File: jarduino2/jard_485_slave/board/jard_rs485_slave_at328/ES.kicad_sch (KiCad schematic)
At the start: 28 parts

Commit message: Re-routage en gagnant de la place (à finir)
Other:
- company: (none) -> BPC
- title: (none) -> Carte de commande d'un Oya par RS485
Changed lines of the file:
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@@
 (kicad_sch (version 20230121) (generator eeschema)
   (paper "A4")
+  (title_block
+    (title "Carte de commande d'un Oya par RS485")
+    (date "2024-03-29")
+    (rev "D0")
+    (company "BPC")
+    (comment 1 "Technologie CMD basée sur ATMEGA328")
+    (comment 2 "Monitoring de tension d'alimentation")
+    (comment 3 "1 sortie 12V/5A - 2 entrées TOR - 1 débimètre - 1 LED - Temp -RS485")
+  )
   (junction (at 60.96 87.63) (diameter 0) (color 0 0 0 0)
   )

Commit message: Petites coquilles de dossier
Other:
- title: Carte de commande d'un Oya par RS485 -> Carte de commande d'un OYA par RS485
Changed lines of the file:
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@@
   (paper "A4")
   (title_block
-    (title "Carte de commande d'un Oya par RS485")
+    (title "Carte de commande d'un OYA par RS485")
     (date "2024-03-29")
     (rev "D0")
     (company "BPC")
-    (comment 1 "Technologie CMD basée sur ATMEGA328")
+    (comment 1 "Technologie CMS basée sur ATMEGA328")
     (comment 2 "Monitoring de tension d'alimentation")
-    (comment 3 "1 sortie 12V/5A - 2 entrées TOR - 1 débimètre - 1 LED - Temp -RS485")
+    (comment 3 "1 sortie 12V/5A - 2 entrées TOR - 1 débimètre - 1 LED - Temp - RS485")
   )
   (junction (at 60.96 87.63) (diameter 0) (color 0 0 0 0)

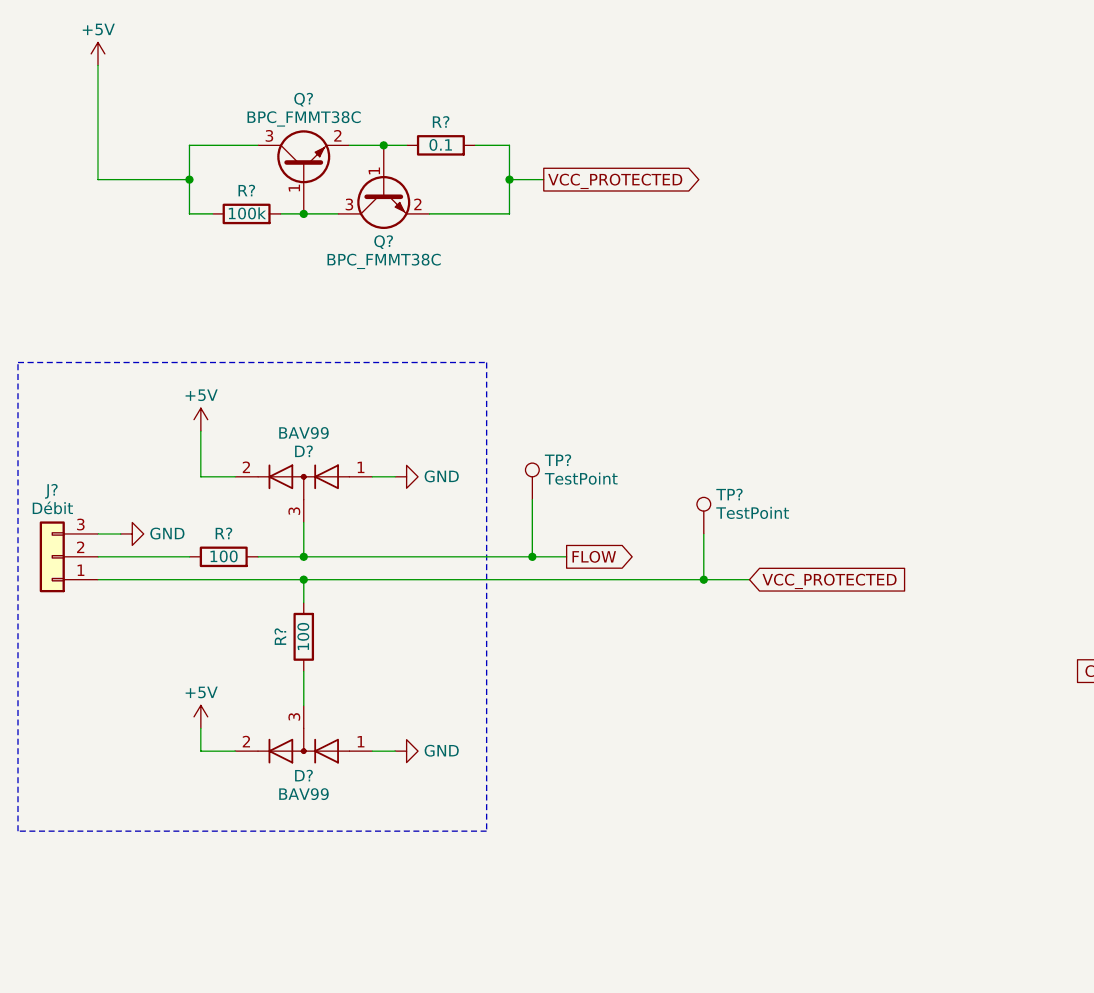
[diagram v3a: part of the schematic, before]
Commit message: Suite revue: - Retrait limiteur de courant NOK pour flowmeter - Résolution des erreurs PCB
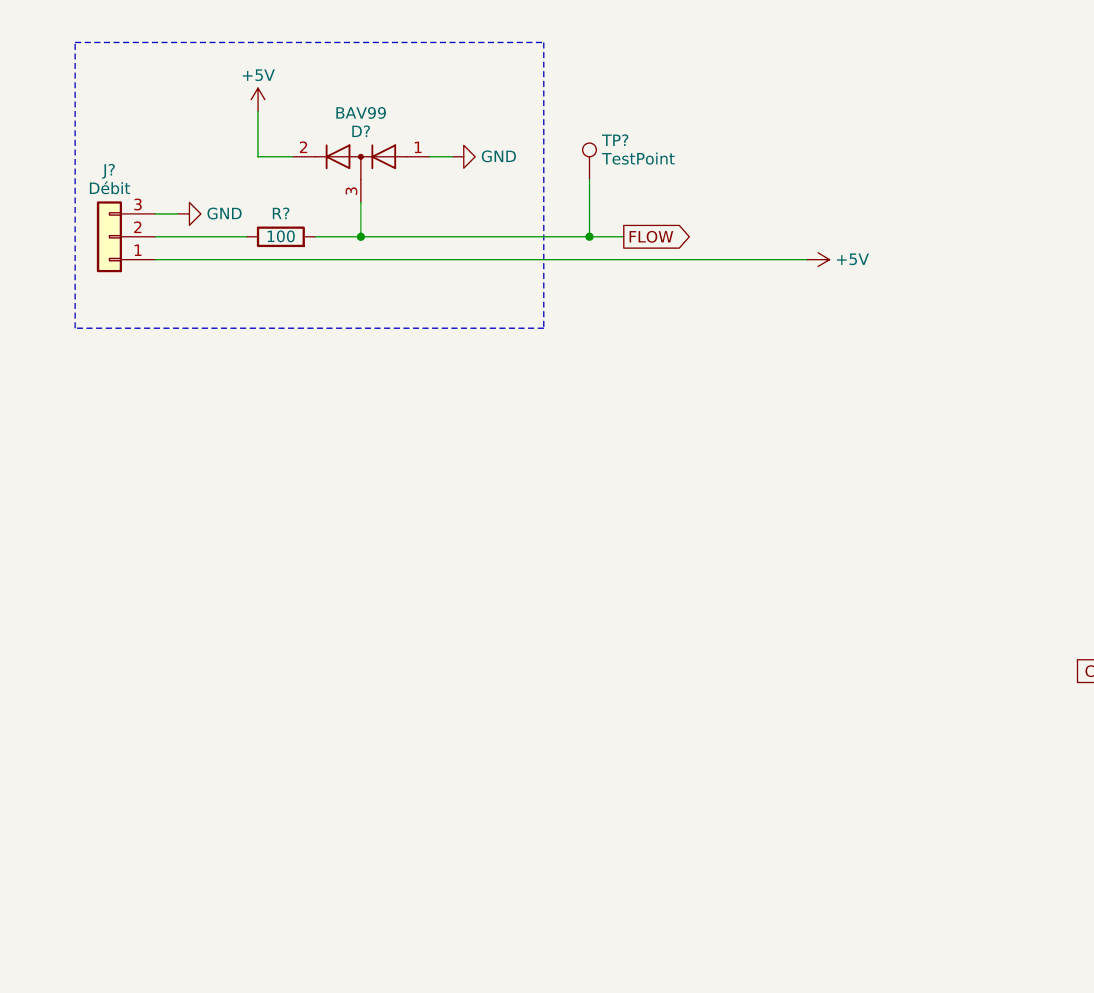
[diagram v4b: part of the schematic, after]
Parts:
- removed D?: BAV99, Package_TO_SOT_SMD:SOT-23, symbol Diode:BAV99
- removed Q? (x2): BPC_FMMT38C, bpc:BPC_SOT-23-3, symbol bpc:BPC_FMMT38C
- removed R?: 100, Resistor_SMD:R_0805_2012Metric_Pad1.20x1.40mm_HandSolder, symbol Device:R
- removed R?: 100k, Resistor_SMD:R_0805_2012Metric_Pad1.20x1.40mm_HandSolder, symbol Device:R
- removed R?: 0.1, Resistor_SMD:R_0805_2012Metric_Pad1.20x1.40mm_HandSolder, symbol Device:R
- removed TP?: TestPoint, TestPoint:TestPoint_Pad_D1.5mm, symbol Connector:TestPoint
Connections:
- net VCC_PROTECTED is gone; now on net +5V: J?.1 (Pin_1)
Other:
- title: Carte de commande d'un OYA par RS485 -> Carte de commande d'un OYA - Esclave RS485
- moved on the sheet: D?, J?, R?, TP?

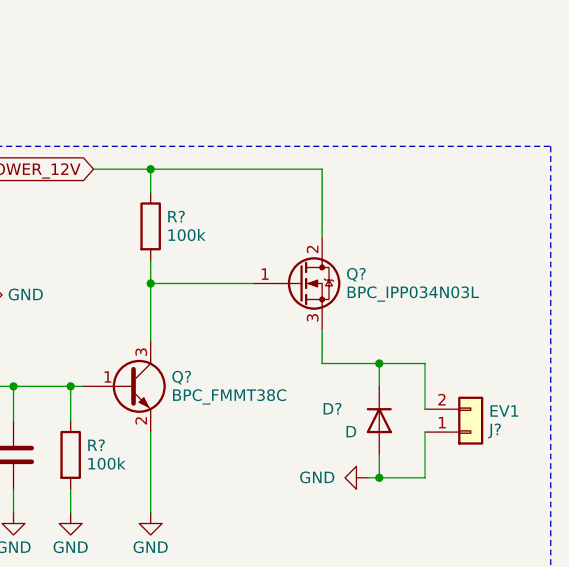
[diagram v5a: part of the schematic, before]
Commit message: Correction erreur de MOS (N au lieu de P) + Saisie complete de la BOM
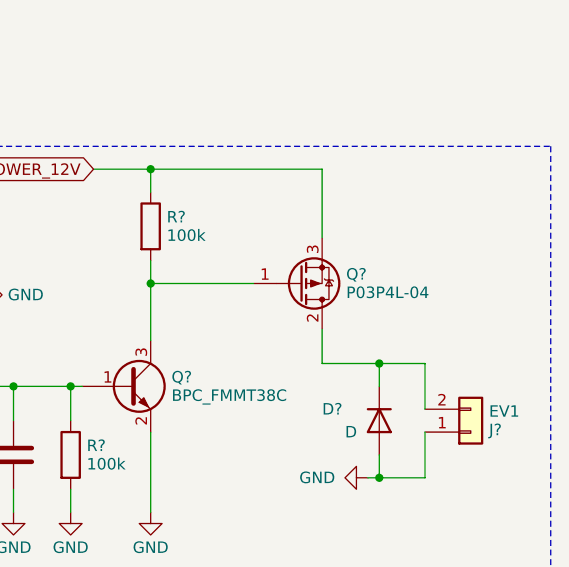
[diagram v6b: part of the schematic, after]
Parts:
- C?: Fabricant (none) -> KEMET; Fournisseur (none) -> Farnell; RefFabricant (none) -> C0603X102J5GACAUTO; RefFournisseur (none) -> 2219417
- D? (x4): Fabricant (none) -> MULTICOMP PRO; Fournisseur (none) -> Farnell; RefFabricant (none) -> BAV99; RefFournisseur (none) -> 2675152
- D?: Fabricant (none) -> MULTICOMP PRO; Fournisseur (none) -> Farnell; RefFabricant (none) -> 1N4007G; RefFournisseur (none) -> 2675047
- J? (x2): Fabricant (none) -> PHOENIX CONTACT; Fournisseur (none) -> Farnell; RefFabricant (none) -> 1725669; RefFournisseur (none) -> 3041360
- J?: Fabricant (none) -> PHOENIX CONTACT; Fournisseur (none) -> Farnell; RefFabricant (none) -> 1725656; RefFournisseur (none) -> 3041359
- Q?: value BPC_IPP034N03L -> P03P4L-04; symbol bpc:BPC_IPP034N03L -> bpc:P03P4L-04; Fabricant (none) -> INFINEON TECHNOLOGIES; RefFabricant (none) -> IPI80P03P4L-04
- Q?: Fabricant (none) -> DIODES; Fournisseur (none) -> Farnell; RefFabricant (none) -> FMMT38C; RefFournisseur (none) -> 9526315
- R? (x3): Fabricant (none) -> VISHAY; Fournisseur (none) -> Farnell; RefFabricant (none) -> CRCW0805100RFKTA; RefFournisseur (none) -> 2826073
- R? (x2): Fabricant (none) -> MULTICOMP PRO; Fournisseur (none) -> Farnell; RefFabricant (none) -> MCHVR05JTEW1003; RefFournisseur (none) -> 2826073
- R?: Fabricant (none) -> MULTICOMP PRO; Fournisseur (none) -> Farnell; RefFabricant (none) -> MCMR06X224 JTL; RefFournisseur (none) -> 2073437
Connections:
- net POWER_12V: now also Q?.3 (S); no longer Q?.2 (D)
- net at D?.1 (K), J?.2 (Pin_2): now also Q?.2 (D); no longer Q?.3 (S)

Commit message: Détails
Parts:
- D?: value D -> 1N4007G
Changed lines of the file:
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@@
       (effects (font (size 1.27 1.27)) (justify left))
     )
-    (property "Value" "D" (at 241.3 102.87 90)
+    (property "Value" "1N4007G" (at 233.68 102.87 90)
       (effects (font (size 1.27 1.27)) (justify left))
     )

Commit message: Ajout des prix des composants
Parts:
- C?: Price (none) -> 0,42
- D? (x4): Price (none) -> 0,0994
- D?: Price (none) -> 0,1272
- J? (x2): Price (none) -> 3,408
- J?: Price (none) -> 2,472
- Q?: Fournisseur (none) -> Radiospares; Price (none) -> 2,707; RefFabricant IPI80P03P4L-04 -> IPP80P03P4L04AKSA1; RefFournisseur (none) -> 823-5554P
- Q?: Price (none) -> 1,1844
- R? (x3): Price (none) -> 0,0522; RefFournisseur 2826073 -> 1652906
- R? (x2): Price (none) -> 0,0522
- R?: Price (none) -> 0,009
- TP? (x4): Price (none) -> 0
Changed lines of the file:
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@@
       (effects (font (size 1.27 1.27)) hide)
     )
-    (property "RefFournisseur" "2826073" (at 52.07 157.48 0)
+    (property "RefFournisseur" "1652906" (at 52.07 157.48 0)
       (effects (font (size 1.27 1.27)) hide)
     )
@@
       (effects (font (size 1.27 1.27)) hide)
     )
+    (property "Price" "0,0522" (at 52.07 157.48 0)
+      (effects (font (size 1.27 1.27)) hide)
+    )
     (pin "1")
     (pin "2")
@@
       (effects (font (size 1.27 1.27)) hide)
     )
-    (property "RefFabricant" "IPI80P03P4L-04" (at 236.22 86.36 0)
-      (effects (font (size 1.27 1.27)) hide)
-    )
-    (property "RefFournisseur" "" (at 236.22 86.36 0)
+    (property "RefFabricant" "IPP80P03P4L04AKSA1" (at 236.22 86.36 0)
+      (effects (font (size 1.27 1.27)) hide)
+    )
+    (property "RefFournisseur" "823-5554P" (at 236.22 86.36 0)
       (effects (font (size 1.27 1.27)) hide)
     )
@@
       (effects (font (size 1.27 1.27)) hide)
     )
+    (property "Fournisseur" "Radiospares" (at 236.22 86.36 0)
+      (effects (font (size 1.27 1.27)) hide)
+    )
+    (property "Price" "2,707" (at 236.22 86.36 0)
+      (effects (font (size 1.27 1.27)) hide)
+    )
     (pin "1")
     (pin "2")
@@
       (effects (font (size 1.27 1.27)) hide)
     )
+    (property "Price" "0,0994" (at 58.42 144.78 0)
+      (effects (font (size 1.27 1.27)) hide)
+    )
     (pin "1")
     (pin "2")
@@
       (effects (font (size 1.27 1.27)) hide)
     )
+    (property "Price" "1,1844" (at 217.17 97.79 0)
+      (effects (font (size 1.27 1.27)) hide)
+    )
     (pin "1")
     (pin "2")
@@
     )
     (property "RefFournisseur" "" (at 104.14 153.67 0)
+      (effects (font (size 1.27 1.27)) hide)
+    )
+    (property "Price" "0" (at 104.14 153.67 0)
       (effects (font (size 1.27 1.27)) hide)
     )
@@
       (effects (font (size 1.27 1.27)) hide)
     )
+    (property "Price" "3,408" (at 39.37 49.53 0)
+      (effects (font (size 1.27 1.27)) hide)
+    )
     (pin "1")
     (pin "2")
@@
       (effects (font (size 1.27 1.27)) hide)
     )
+    (property "Price" "0" (at 86.36 153.67 0)
+      (effects (font (size 1.27 1.27)) hide)
+    )
     (pin "1")
     (instances
@@
     )
     (property "Description" "Résistance 100 kOhms" (at 210.82 105.41 0)
+      (effects (font (size 1.27 1.27)) hide)
+    )
+    (property "Price" "0,0522" (at 210.82 105.41 0)
       (effects (font (size 1.27 1.27)) hide)
     )
@@
       (effects (font (size 1.27 1.27)) hide)
     )
+    (property "Price" "0,0994" (at 67.31 40.64 0)
+      (effects (font (size 1.27 1.27)) hide)
+    )
     (pin "1")
     (pin "2")
@@
       (effects (font (size 1.27 1.27)) hide)
     )
-    (property "RefFournisseur" "2826073" (at 52.07 160.02 0)
+    (property "RefFournisseur" "1652906" (at 52.07 160.02 0)
       (effects (font (size 1.27 1.27)) hide)
     )
@@
       (effects (font (size 1.27 1.27)) hide)
     )
+    (property "Price" "0,0522" (at 52.07 160.02 0)
+      (effects (font (size 1.27 1.27)) hide)
+    )
     (pin "1")
     (pin "2")
@@
     )
     (property "Description" "Bornier 3 contacts 2.54mm" (at 40.64 157.48 0)
+      (effects (font (size 1.27 1.27)) hide)
+    )
+    (property "Price" "3,408" (at 40.64 157.48 0)
       (effects (font (size 1.27 1.27)) hide)
     )
@@
       (effects (font (size 1.27 1.27)) hide)
     )
+    (property "Price" "2,472" (at 255.27 102.87 0)
+      (effects (font (size 1.27 1.27)) hide)
+    )
     (pin "1")
     (pin "2")
@@
     )
     (property "Description" "Résistance 100 kOhms" (at 219.71 80.01 0)
+      (effects (font (size 1.27 1.27)) hide)
+    )
+    (property "Price" "0,0522" (at 219.71 80.01 0)
       (effects (font (size 1.27 1.27)) hide)
     )
@@
       (effects (font (size 1.27 1.27)) hide)
     )
+    (property "Price" "0,0994" (at 58.42 168.91 0)
+      (effects (font (size 1.27 1.27)) hide)
+    )
     (pin "1")
     (pin "2")
@@
     )
     (property "RefFournisseur" "" (at 92.71 43.18 0)
+      (effects (font (size 1.27 1.27)) hide)
+    )
+    (property "Price" "0" (at 92.71 43.18 0)
       (effects (font (size 1.27 1.27)) hide)
     )
@@
       (effects (font (size 1.27 1.27)) hide)
     )
+    (property "Price" "0,42" (at 204.47 105.41 0)
+      (effects (font (size 1.27 1.27)) hide)
+    )
     (pin "1")
     (pin "2")
@@
     )
     (property "Description" "Résistance 220 Ohms" (at 198.12 97.79 0)
+      (effects (font (size 1.27 1.27)) hide)
+    )
+    (property "Price" "0,009" (at 198.12 97.79 0)
       (effects (font (size 1.27 1.27)) hide)
     )
@@
       (effects (font (size 1.27 1.27)) hide)
     )
-    (property "RefFournisseur" "2826073" (at 58.42 49.53 0)
+    (property "RefFournisseur" "1652906" (at 58.42 49.53 0)
       (effects (font (size 1.27 1.27)) hide)
     )
@@
       (effects (font (size 1.27 1.27)) hide)
     )
+    (property "Price" "0,0522" (at 58.42 49.53 0)
+      (effects (font (size 1.27 1.27)) hide)
+    )
     (pin "1")
     (pin "2")
@@
     )
     (property "RefFournisseur" "" (at 160.02 91.44 0)
+      (effects (font (size 1.27 1.27)) hide)
+    )
+    (property "Price" "0" (at 160.02 91.44 0)
       (effects (font (size 1.27 1.27)) hide)
     )
@@
       (effects (font (size 1.27 1.27)) hide)
     )
+    (property "Price" "0,0994" (at 186.69 87.63 0)
+      (effects (font (size 1.27 1.27)) hide)
+    )
     (pin "1")
     (pin "2")
@@
       (effects (font (size 1.27 1.27)) hide)
     )
+    (property "Price" "0,1272" (at 245.11 101.6 0)
+      (effects (font (size 1.27 1.27)) hide)
+    )
